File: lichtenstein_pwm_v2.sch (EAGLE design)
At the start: 60 parts, among them IC2 MCP23017, IC3 74AHCT125SOIC14, IC5 LM75B, J1 MAGJACK, U1 ONION-OMEGA2

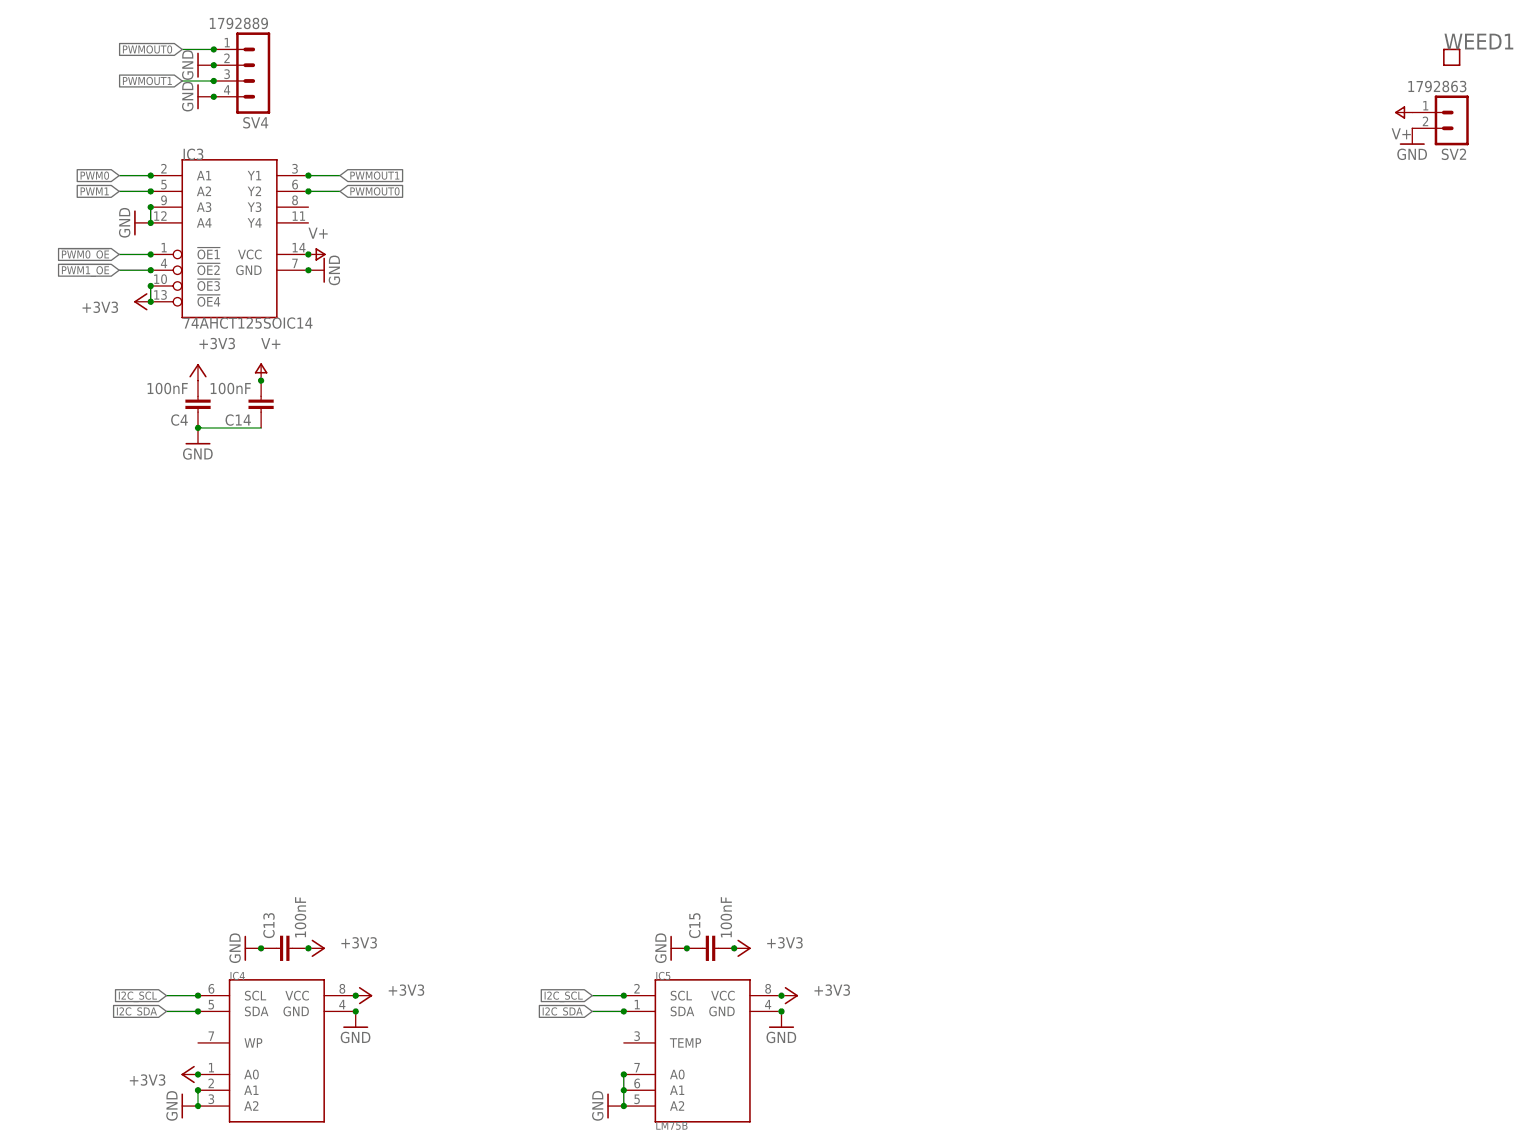
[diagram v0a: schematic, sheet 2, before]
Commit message: power for pwm board
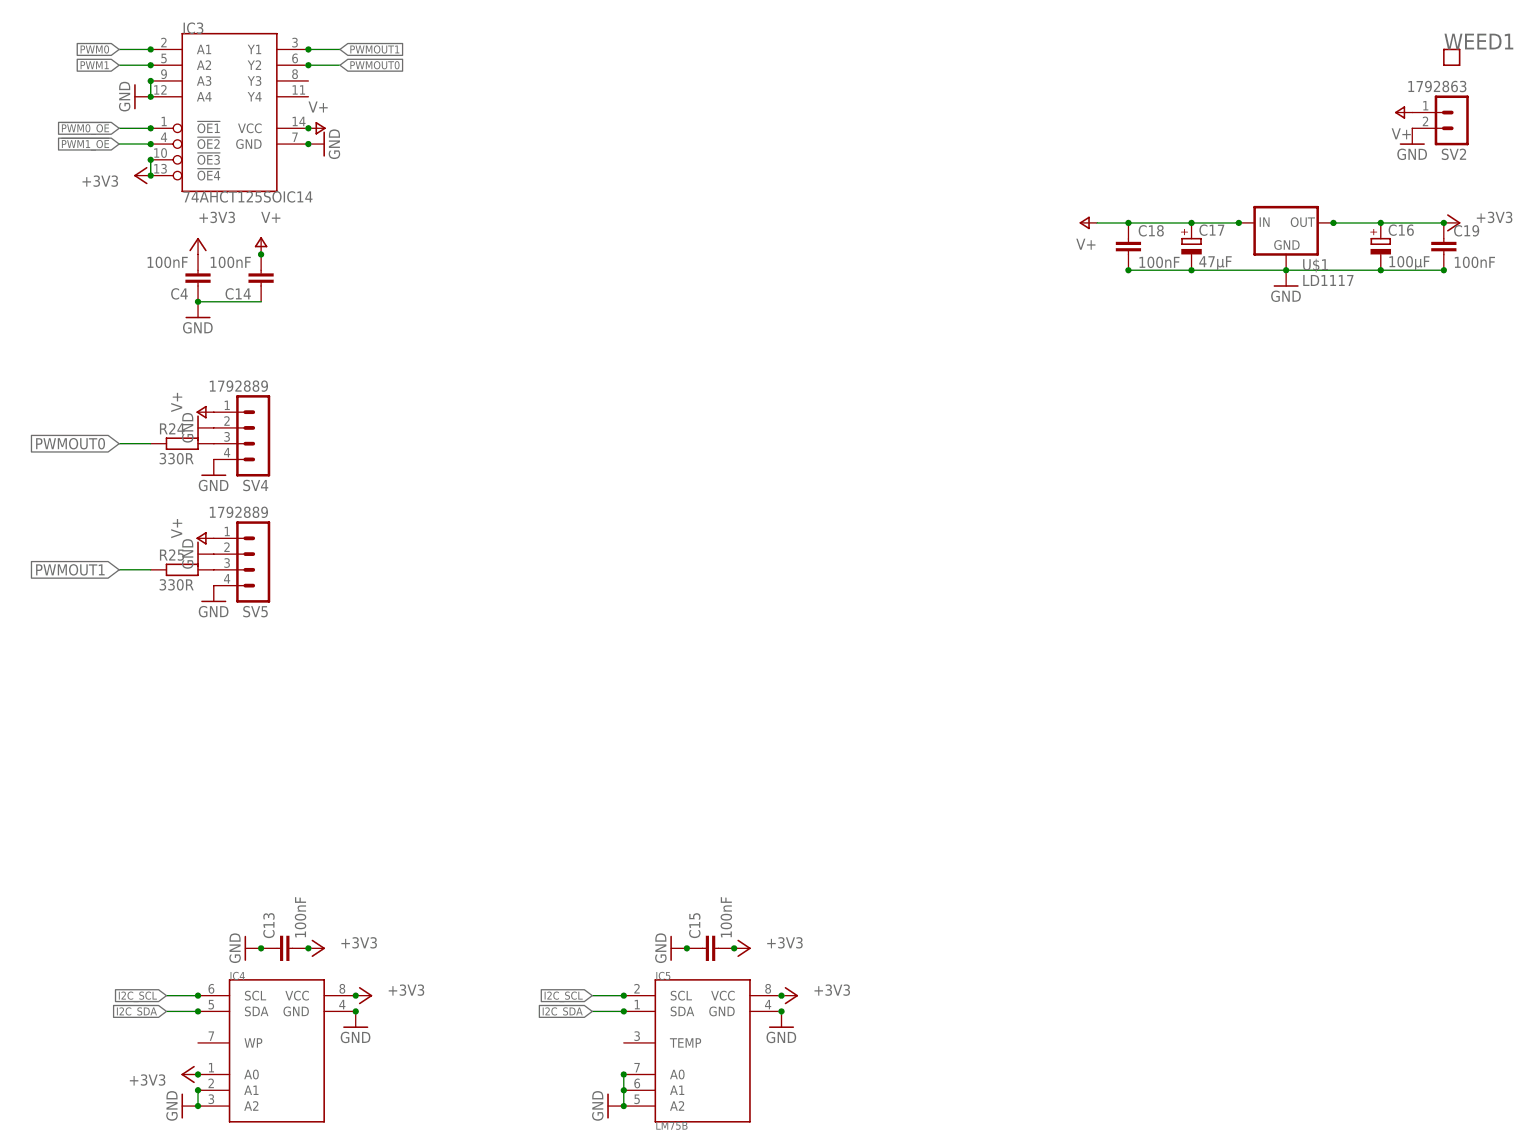
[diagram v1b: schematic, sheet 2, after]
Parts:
- removed C1, C7: 100nF, rcl:C-EUC0805
- removed C3: 47µF, rcl:CPOL-EUCT7343
- removed C6: 100µF, rcl:CPOL-EUCT7343
- added C16: 100µF, rcl:CPOL-EUCT7343
- added C17: 47µF, rcl:CPOL-EUCT7343
- added C18, C19: 100nF, rcl:C-EUC0805
- added R24, R25: 330R, rcl:R-EU_M0805
- added SV5: 1792889, lichtenstein_onion:1792889
- added U$1: LD1117, lichtenstein_onion:LD1117TO-220
- SV1: device con-lstb:MA06-1 -> con-lstb:MA03-1
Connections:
- new net N$7: R24.2, SV4.3
- new net N$8: R25.2, SV5.3
- net +3V3: now also C16.+, C19.1, U$1.OUT; no longer C6.+, C7.1, SV1.3
- net CONSOLE_RX: now also SV1.3; no longer SV1.5
- net CONSOLE_TX: now also SV1.2; no longer SV1.4
- net GND: now also C16.-, C17.-, C18.2, C19.2, SV5.2, SV5.4, U$1.GND; no longer C1.2, C3.-, C6.-, C7.2
- net PWMOUT0: now also R24.1; no longer SV4.1
- net PWMOUT1: now also R25.1; no longer SV4.3
- net V+: now also C17.+, C18.1, SV4.1, SV5.1, U$1.IN; no longer C1.1, C3.+
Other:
- note removed: "FTDI Header"
- moved on the sheet: C14, C4, IC3, SV4

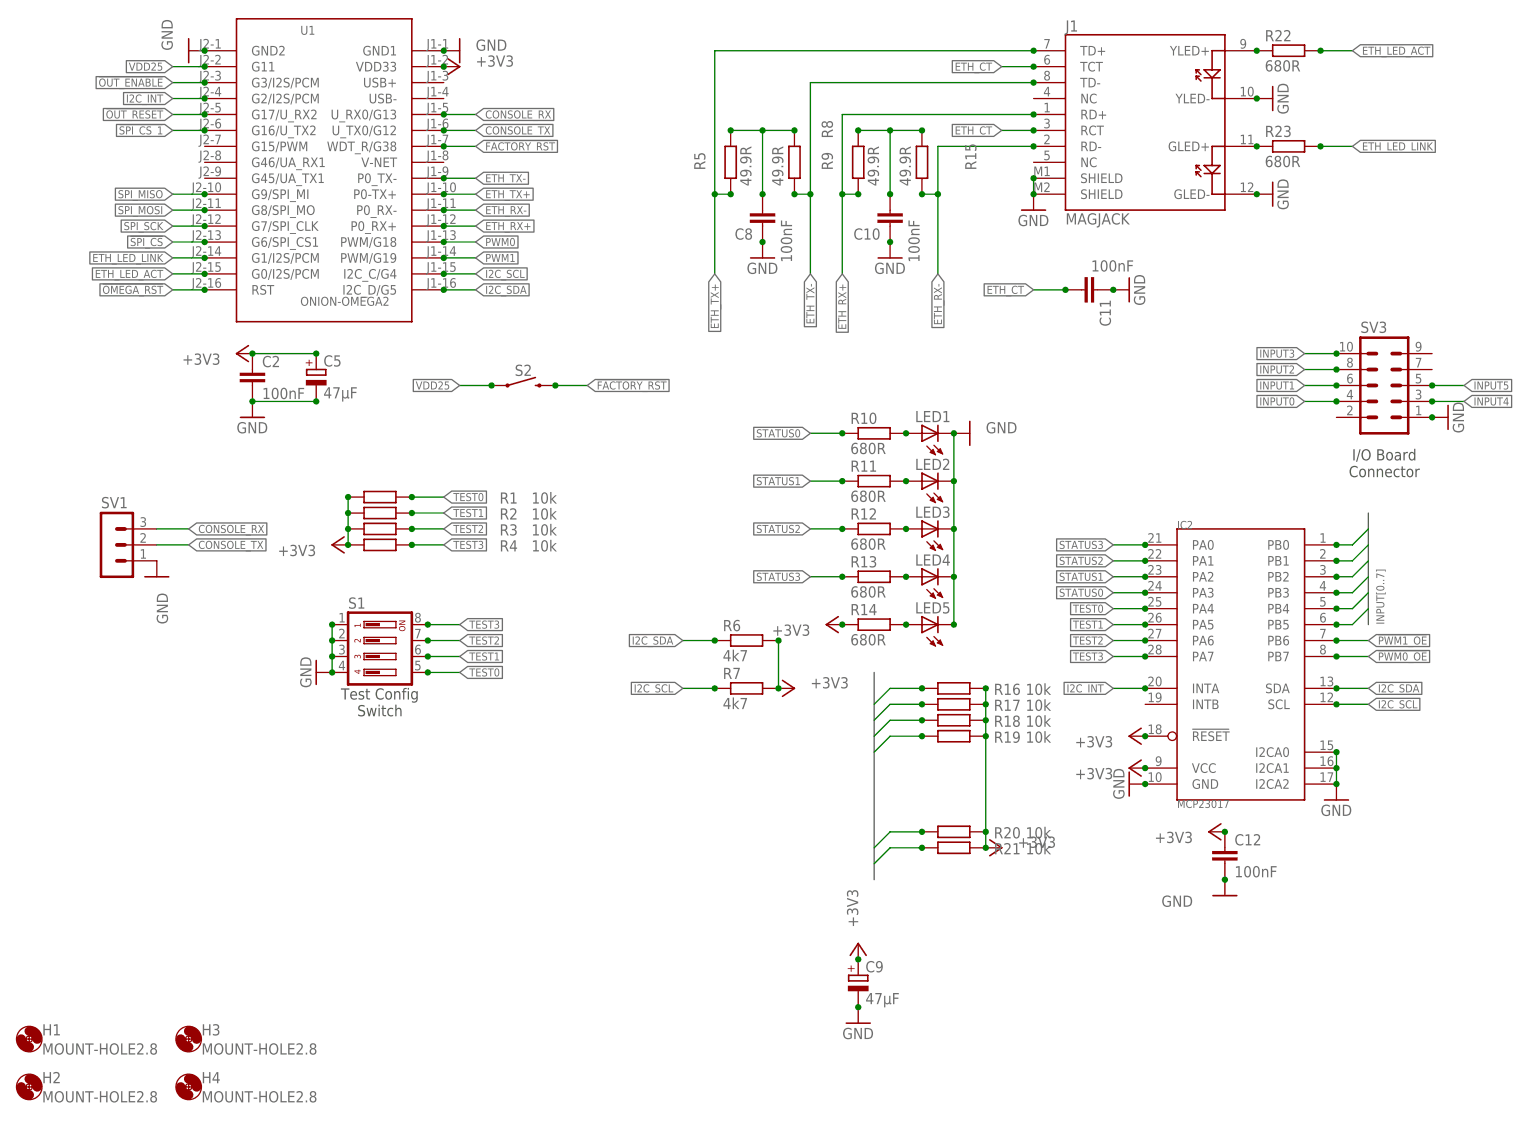
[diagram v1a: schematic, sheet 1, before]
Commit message: routed most of the pwm board, need to finish with input connectors
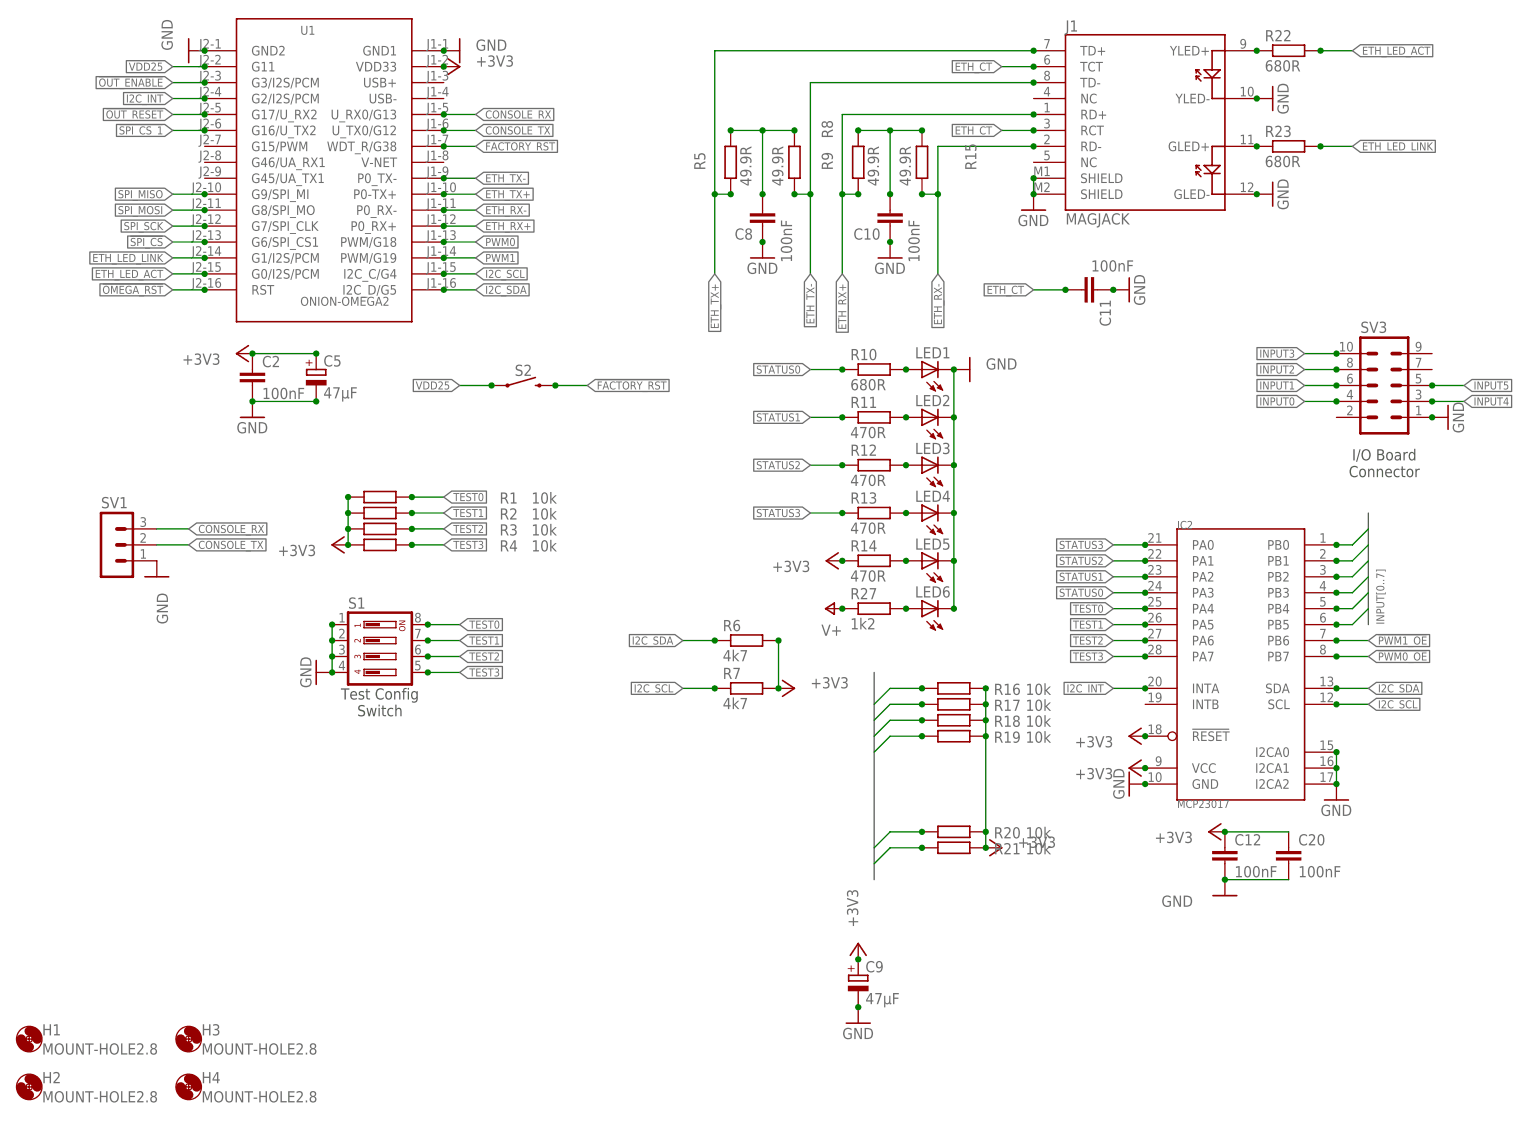
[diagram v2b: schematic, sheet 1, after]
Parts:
- added C1, C20, C3, C6, C7: 100nF, rcl:C-EUC0805
- added IC1: MAX11647, lichtenstein_onion:MAX11647UMAX-8
- added LED6: (no value), led:LEDCHIPLED_1206
- added R26: 2k, rcl:R-EU_M0805
- added R27: 1k2, rcl:R-EU_M0805
- added R28: 3k09, rcl:R-EU_M0805
- added R29: 1k07, rcl:R-EU_M0805
- IC2: device lichtenstein_onion:MCP23017SSOP28 -> lichtenstein_onion:MCP23017SOIC28
- R10: MOUSER 652-CR0805-FX6800GLF -> 667-ERJ-6ENF6800V
- R11, R12, R13, R14: value 680R -> 470R; MOUSER 652-CR0805-FX6800GLF -> 652-CR0805JW-471ELF
- renumbered U$1 to IC9
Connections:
- new net CURRENT: IC1.AIN1
- new net N$12: IC1.REF, R26.1
- new net N$13: C3.2, R26.2
- new net N$14: LED6.A, R27.2
- new net VIN_DIVIDED: IC1.AIN0, R28.1, R29.2
- net +3V3: now also C1.2, C20.1, IC1.VCC
- net GND: now also C1.1, C20.2, C3.1, C6.2, C7.2, IC1.GND, IC4.WP, LED6.C, R29.1
- net I2C_SCL: now also IC1.SCL
- net I2C_SDA: now also IC1.SDA
- net TEST0: now also S1.8; no longer S1.5
- net TEST1: now also S1.7; no longer S1.6
- net TEST2: now also S1.6; no longer S1.7
- net TEST3: now also S1.5; no longer S1.8
- net V+: now also C6.1, C7.1, R27.1, R28.2
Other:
- moved on the sheet: LED1, LED2, LED3, LED4, LED5, R10, R11, R12, R13, R14

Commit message: finished routing PWMv2 board
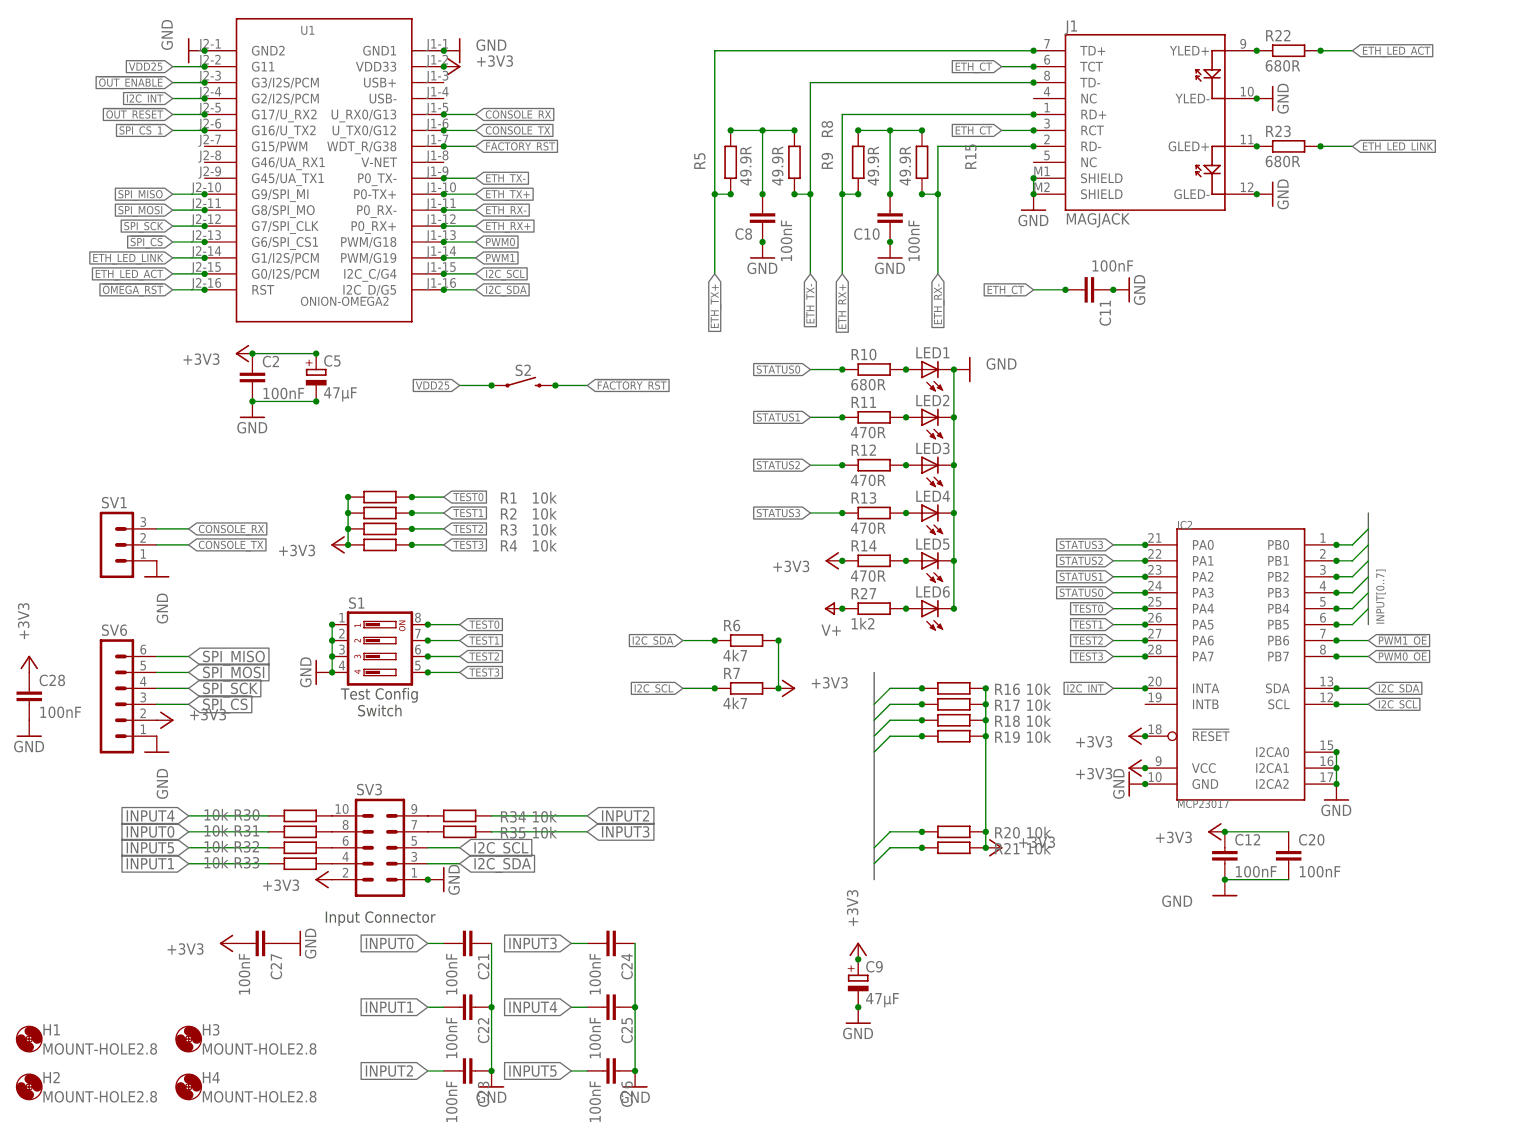
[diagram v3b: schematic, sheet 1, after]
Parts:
- added C21, C22, C23, C24, C25, C26, C27, C28: 100nF, rcl:C-EUC0805
- added R30, R31, R32, R33, R34, R35: 10k, rcl:R-EU_M0805
- added SV6: (no value), con-lstb:MA06-1
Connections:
- new net N$15: R30.1, SV3.10
- new net N$16: R31.1, SV3.8
- new net N$17: R32.1, SV3.6
- new net N$18: R33.1, SV3.4
- new net N$19: R34.1, SV3.9
- new net N$20: R35.1, SV3.7
- net !SPI_CS: now also SV6.3
- net +3V3: now also C27.2, C28.1, SV3.2, SV6.2
- net GND: now also C21.1, C22.1, C23.1, C24.1, C25.1, C26.1, C27.1, C28.2, SV6.1
- net I2C_SCL: now also SV3.5
- net I2C_SDA: now also SV3.3
- net INPUT0: now also C21.2, R31.2; no longer SV3.4
- net INPUT1: now also C22.2, R33.2; no longer SV3.6
- net INPUT2: now also C23.2, R34.2; no longer SV3.8
- net INPUT3: now also C24.2, R35.2; no longer SV3.10
- net INPUT4: now also C25.2, R30.2; no longer SV3.3
- net INPUT5: now also C26.2, R32.2; no longer SV3.5
- net SPI_MISO: now also SV6.6
- net SPI_MOSI: now also SV6.5
- net SPI_SCK: now also SV6.4
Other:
- note added: "Input Connector"
- note removed: "I/O Board Connector"
- moved on the sheet: SV3
